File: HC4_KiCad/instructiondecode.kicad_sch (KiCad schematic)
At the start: 64 parts, among them IC18 74HC74, IC19 74HC32, IC20 74HC04, IC21 74HC00, IC22 74HC4053, IC23 74HC151, IC9 74HC4002

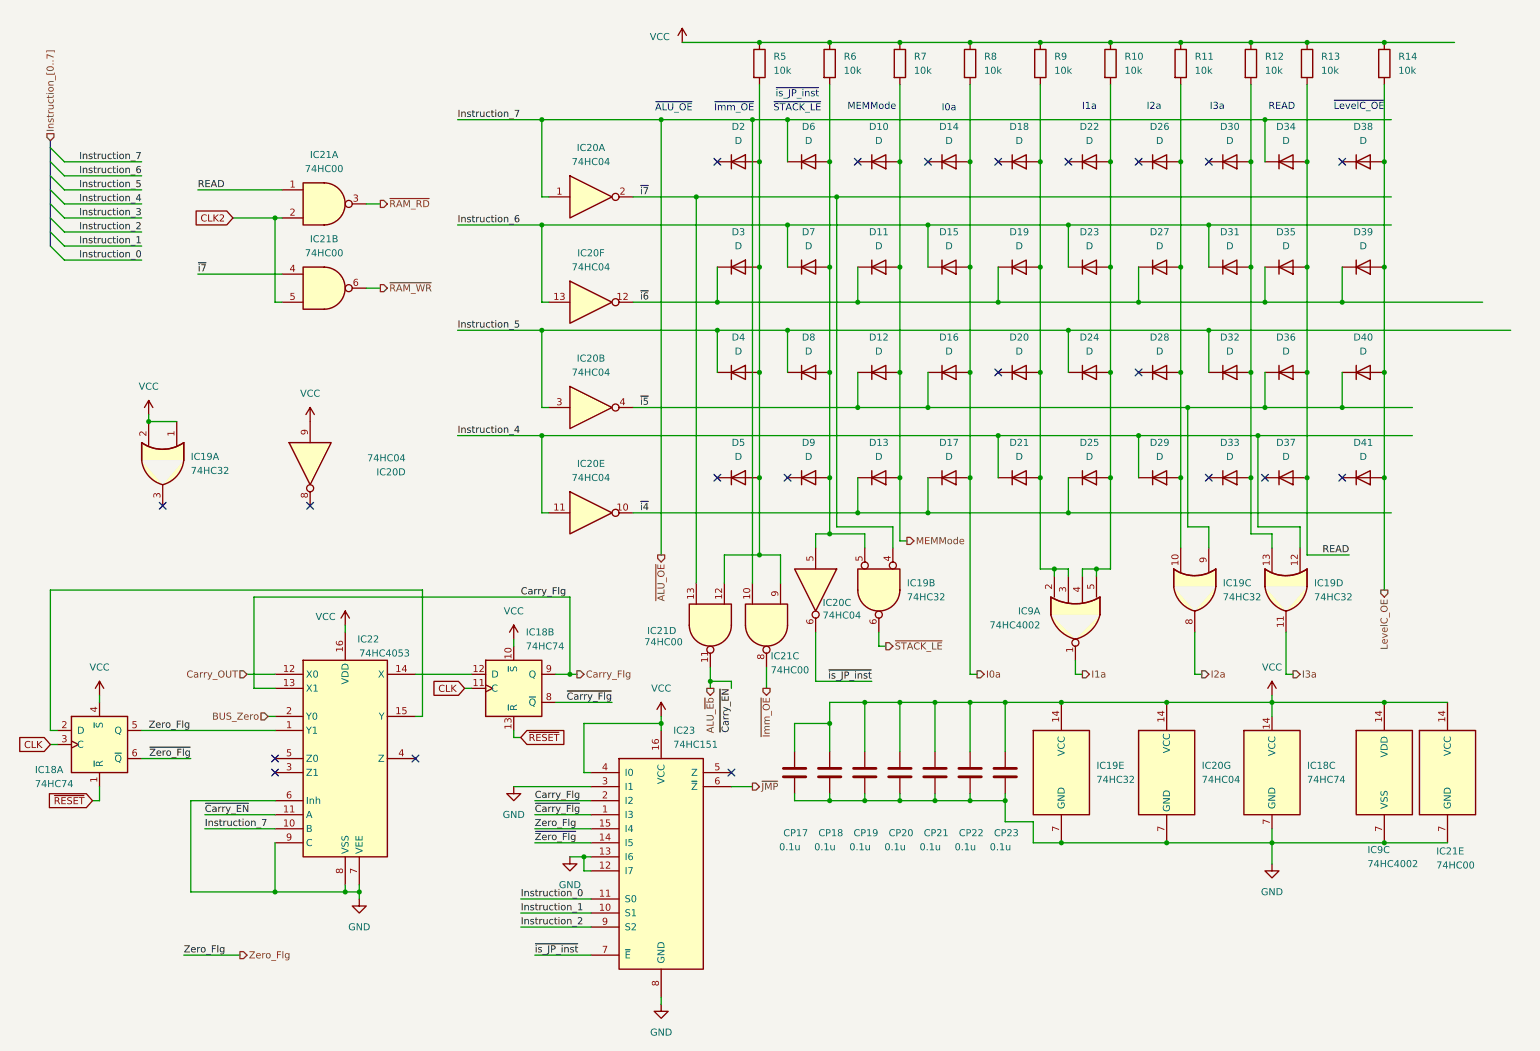
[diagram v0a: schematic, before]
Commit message: 部品配置完了
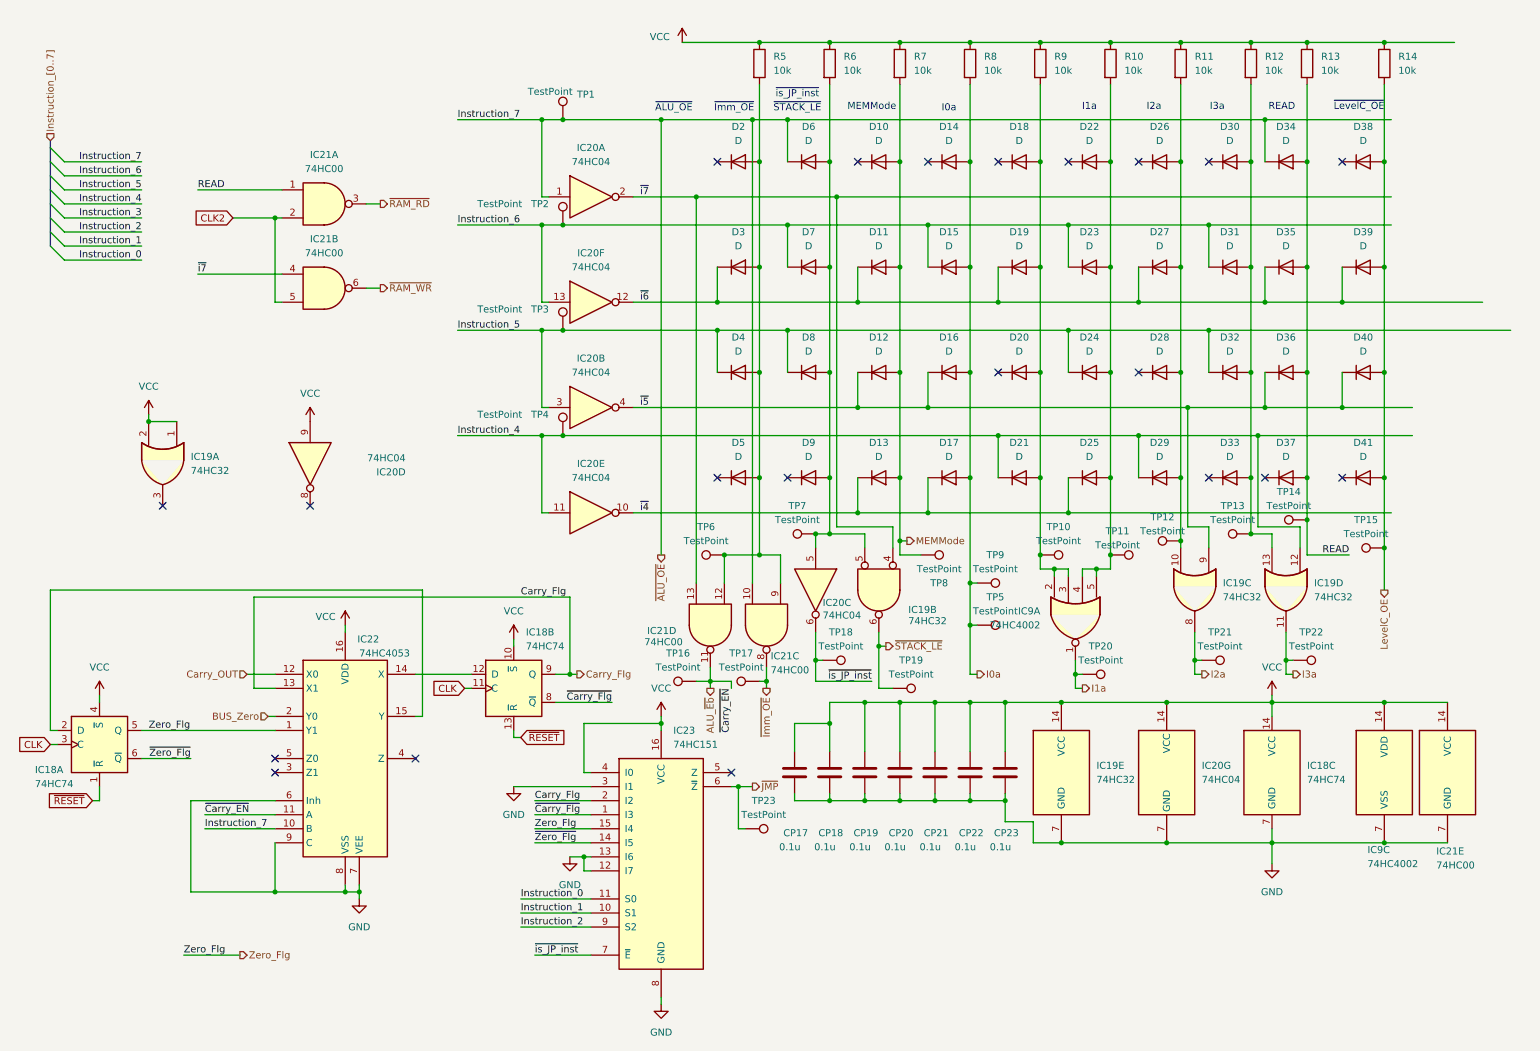
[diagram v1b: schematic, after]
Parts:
- added TP1, TP10, TP11, TP12, TP13, TP14, TP15, TP16, TP17, TP18, TP19, TP2, TP20, TP21, TP22, TP23, TP3, TP4, TP5, TP6, TP7, TP8, TP9: TestPoint, Library:TestPoint_THTPad_1.0x1.0mm_Drill0.5mm, symbol Connector:TestPoint
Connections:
- net ALU_~{Eb}: now also TP16.1
- net I0a: now also TP5.1, TP9.1
- net I1a: now also TP20.1
- net I2a: now also TP21.1
- net I3a: now also TP22.1
- net Instruction_4: now also TP4.1
- net Instruction_5: now also TP3.1
- net Instruction_6: now also TP2.1
- net LevelC_OE: now also TP15.1
- net MEMMode: now also TP8.1
- net READ: now also TP14.1
- net ~{ALU_OE}: now also TP1.1
- net ~{Imm_OE}: now also TP17.1
- net ~{JMP}: now also TP23.1
- net ~{STACK_LE}: now also TP19.1
- net ~{is_JP_inst}: now also TP18.1
- net at D26.2 (A), D27.2 (A), D28.2 (A)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: now also TP12.1
- net at D30.2 (A), D31.2 (A), D32.2 (A)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: now also TP13.1
- net at D2.2 (A), D3.2 (A), D4.2 (A)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: now also TP6.1
- net at D6.2 (A), D7.2 (A), D8.2 (A)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: now also TP7.1
- net at D22.2 (A), D23.2 (A), D24.2 (A)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: now also TP11.1
- net at D18.2 (A), D19.2 (A), D20.2 (A)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: now also TP10.1

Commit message: 配線完了とみられる
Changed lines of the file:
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@@
 (kicad_sch
-	(version 20231120)
+	(version 20250114)
 	(generator "eeschema")
-	(generator_version "8.0")
+	(generator_version "9.0")
 	(paper "A4")
 	(title_block
@@
 		(rev "1.3")
 	)
+	(text "I2a"
+		(exclude_from_sim no)
+		(at 219.964 28.194 0)
+		(effects
+			(font
+				(size 1.27 1.27)
+			)
+		)
+	)
+	(text "I0a"
+		(exclude_from_sim no)
+		(at 182.88 28.448 0)
+		(effects
+			(font
+				(size 1.27 1.27)
+			)
+		)
+	)
+	(text "~{Imm_OE}"
+		(exclude_from_sim no)
+		(at 144.018 28.448 0)
+		(effects
+			(font
+				(size 1.27 1.27)
+			)
+		)
+	)
+	(text "~{LevelC_OE}"
+		(exclude_from_sim no)
+		(at 257.048 28.194 0)
+		(effects
+			(font
+				(size 1.27 1.27)
+			)
+		)
+	)
+	(text "~{ALU_OE}"
+		(exclude_from_sim no)
+		(at 133.096 28.448 0)
+		(effects
+			(font
+				(size 1.27 1.27)
+			)
+		)
+	)
+	(text "~{STACK_LE}"
+		(exclude_from_sim no)
+		(at 155.448 28.448 0)
+		(effects
+			(font
+				(size 1.27 1.27)
+			)
+		)
+	)
+	(text "I3a"
+		(exclude_from_sim no)
+		(at 231.394 28.194 0)
+		(effects
+			(font
+				(size 1.27 1.27)
+			)
+		)
+	)
+	(text "READ"
+		(exclude_from_sim no)
+		(at 243.078 28.194 0)
+		(effects
+			(font
+				(size 1.27 1.27)
+			)
+		)
+	)
+	(text "MEMMode"
+		(exclude_from_sim no)
+		(at 168.91 28.194 0)
+		(effects
+			(font
+				(size 1.27 1.27)
+			)
+		)
+	)
+	(text "I1a"
+		(exclude_from_sim no)
+		(at 208.28 28.194 0)
+		(effects
+			(font
+				(size 1.27 1.27)
+			)
+		)
+	)
+	(text "~{is_JP_inst}"
+		(exclude_from_sim no)
+		(at 155.448 25.908 0)
+		(effects
+			(font
+				(size 1.27 1.27)
+			)
+		)
+	)
 	(junction
 		(at 167.64 135.89)
@@
 		)
 	)
-	(text "I2a"
-		(exclude_from_sim no)
-		(at 219.964 28.194 0)
-		(effects
-			(font
-				(size 1.27 1.27)
-			)
-		)
-	)
-	(text "I0a"
-		(exclude_from_sim no)
-		(at 182.88 28.448 0)
-		(effects
-			(font
-				(size 1.27 1.27)
-			)
-		)
-	)
-	(text "~{Imm_OE}"
-		(exclude_from_sim no)
-		(at 144.018 28.448 0)
-		(effects
-			(font
-				(size 1.27 1.27)
-			)
-		)
-	)
-	(text "~{LevelC_OE}"
-		(exclude_from_sim no)
-		(at 257.048 28.194 0)
-		(effects
-			(font
-				(size 1.27 1.27)
-			)
-		)
-	)
-	(text "~{ALU_OE}"
-		(exclude_from_sim no)
-		(at 133.096 28.448 0)
-		(effects
-			(font
-				(size 1.27 1.27)
-			)
-		)
-	)
-	(text "~{STACK_LE}"
-		(exclude_from_sim no)
-		(at 155.448 28.448 0)
-		(effects
-			(font
-				(size 1.27 1.27)
-			)
-		)
-	)
-	(text "I3a"
-		(exclude_from_sim no)
-		(at 231.394 28.194 0)
-		(effects
-			(font
-				(size 1.27 1.27)
-			)
-		)
-	)
-	(text "READ"
-		(exclude_from_sim no)
-		(at 243.078 28.194 0)
-		(effects
-			(font
-				(size 1.27 1.27)
-			)
-		)
-	)
-	(text "MEMMode"
-		(exclude_from_sim no)
-		(at 168.91 28.194 0)
-		(effects
-			(font
-				(size 1.27 1.27)
-			)
-		)
-	)
-	(text "I1a"
-		(exclude_from_sim no)
-		(at 208.28 28.194 0)
-		(effects
-			(font
-				(size 1.27 1.27)
-			)
-		)
-	)
-	(text "~{is_JP_inst}"
-		(exclude_from_sim no)
-		(at 155.448 25.908 0)
-		(effects
-			(font
-				(size 1.27 1.27)
-			)
-		)
-	)

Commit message: ミスを修正
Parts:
- removed unit 5 of IC21
- added unit 5 of IC5
- renumbered CP17 to CP1, CP18 to CP2, CP19 to CP3, CP20 to CP4, CP21 to CP5, CP22 to CP6, CP23 to CP7, D2 to D1, D11 to D10, D12 to D11, D13 to D12, D14 to D13, D15 to D14, D16 to D15, D17 to D16, D18 to D17, D19 to D18, D20 to D19, D3 to D2, D21 to D20, D22 to D21, D23 to D22, D24 to D23, D25 to D24, D26 to D25, D27 to D26, D28 to D27, D29 to D28, D30 to D29, D4 to D3, D31 to D30, D32 to D31, D33 to D32, D34 to D33, D35 to D34, D36 to D35, D37 to D36, D38 to D37, D39 to D38, D40 to D39, D5 to D4, D41 to D40, D6 to D5, D7 to D6, D8 to D7, D9 to D8, D10 to D9, IC18 to IC2, IC19 to IC3, IC20 to IC4, IC21 to IC5, IC22 to IC6, IC23 to IC7, IC9 to IC8, R5 to R1, R14 to R10, R6 to R2, R7 to R3, R8 to R4, R9 to R5, R10 to R6, R11 to R7, R12 to R8, R13 to R9, TP18 to TP10, TP19 to TP11, TP8 to TP12, TP9 to TP13, TP5 to TP14, TP10 to TP15, TP20 to TP16, TP11 to TP17, TP12 to TP18, TP21 to TP19, TP13 to TP20, TP22 to TP21, TP14 to TP22, TP15 to TP23, TP16 to TP5, TP23 to TP7, TP17 to TP8, TP7 to TP9
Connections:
- net ALU_~{Eb}: now also IC5.3; no longer IC5.11
- net CLK2: now also IC5.10, IC5.13; no longer IC5.2, IC5.5
- net GND: now also IC5.7 (GND)
- net Instruction_5: now also D15.1 (K)
- net Instruction_6: no longer D14.1 (K)
- net READ: now also IC5.9; no longer IC5.1
- net VCC: now also IC4.5, IC5.14 (VCC); no longer IC4.9
- net ~{ALU_OE}: now also IC5.5; no longer IC5.10
- net ~{Imm_OE}: now also IC5.6; no longer IC5.8
- net ~{RAM_RD}: now also IC5.8; no longer IC5.3
- net ~{RAM_WR}: now also IC5.11; no longer IC5.6
- net ~{i5}: no longer D15.1 (K)
- net ~{i6}: now also D14.1 (K)
- net ~{i7}: now also IC5.12, IC5.2; no longer IC5.13, IC5.4
- net ~{is_JP_inst}: now also IC4.8; no longer IC4.6
- net at D1.2 (A), D2.2 (A), D3.2 (A)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: now also IC5.1, IC5.4; no longer IC5.12, IC5.9
- net at D5.2 (A), D6.2 (A), D7.2 (A)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: now also IC4.9; no longer IC4.5

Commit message: なんか変わってた
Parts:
- renumbered CP1 to CP17, CP2 to CP18, CP3 to CP19, CP4 to CP20, CP5 to CP21, CP6 to CP22, CP7 to CP23, D9 to D10, D10 to D11, D11 to D12, D12 to D13, D13 to D14, D14 to D15, D15 to D16, D16 to D17, D17 to D18, D18 to D19, D1 to D2, D19 to D20, D20 to D21, D21 to D22, D22 to D23, D23 to D24, D24 to D25, D25 to D26, D26 to D27, D27 to D28, D28 to D29, D2 to D3, D29 to D30, D30 to D31, D31 to D32, D32 to D33, D33 to D34, D34 to D35, D35 to D36, D36 to D37, D37 to D38, D38 to D39, D3 to D4, D39 to D40, D40 to D41, D4 to D5, D5 to D6, D6 to D7, D7 to D8, D8 to D9, IC2 to IC18, IC3 to IC19, IC4 to IC20, IC5 to IC21, IC6 to IC22, IC7 to IC23, IC8 to IC9, R6 to R10, R7 to R11, R8 to R12, R9 to R13, R10 to R14, R1 to R5, R2 to R6, R3 to R7, R4 to R8, R5 to R9
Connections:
- net ALU_~{Eb}: now also IC21.11; no longer IC21.3
- net CLK2: now also IC21.2, IC21.5; no longer IC21.10, IC21.13
- net READ: now also IC21.1; no longer IC21.9
- net VCC: now also IC20.9; no longer IC20.5
- net ~{ALU_OE}: now also IC21.10; no longer IC21.5
- net ~{Imm_OE}: now also IC21.8; no longer IC21.6
- net ~{RAM_RD}: now also IC21.3; no longer IC21.8
- net ~{RAM_WR}: now also IC21.6; no longer IC21.11
- net ~{i7}: now also IC21.13, IC21.4; no longer IC21.12, IC21.2
- net ~{is_JP_inst}: now also IC20.6; no longer IC20.8
- net at D2.2 (A), D3.2 (A), D4.2 (A)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: now also IC21.12, IC21.9; no longer IC21.1, IC21.4
- net at D6.2 (A), D7.2 (A), D8.2 (A)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: now also IC20.5; no longer IC20.9

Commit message: moti
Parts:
- removed R10, R11, R12, R5, R6, R7, R8, R9: 10k, Resistor_SMD:R_0603_1608Metric, symbol Device:R
- added RN7: 10k, Resistor_THT:R_Array_SIP9, symbol Device:R_Network08_Split
- IC17: renamed from IC18; footprint Package_SO:SO-14_5.3x10.2mm_P1.27mm -> Package_DIP:DIP-14_W7.62mm
- IC18: renamed from IC19; footprint Package_SO:SO-14_5.3x10.2mm_P1.27mm -> Package_DIP:DIP-14_W7.62mm
- IC19: renamed from IC20; footprint Package_SO:SO-14_5.3x10.2mm_P1.27mm -> Package_DIP:DIP-14_W7.62mm
- IC20: renamed from IC21; footprint Package_SO:SO-14_5.3x10.2mm_P1.27mm -> Package_DIP:DIP-14_W7.62mm
- IC21: renamed from IC22; footprint Package_SO:SO-16_5.3x10.2mm_P1.27mm -> Package_DIP:DIP-16_W7.62mm
- IC22: renamed from IC23; footprint Package_SO:SO-16_5.3x10.2mm_P1.27mm -> Package_DIP:DIP-16_W7.62mm
- IC8: renamed from IC9; footprint Package_SO:SO-14_5.3x10.2mm_P1.27mm -> Package_DIP:DIP-14_W7.62mm
- renumbered CP17 to CP16, CP18 to CP17, CP19 to CP18, CP20 to CP19, CP21 to CP20, CP22 to CP21, CP23 to CP22, R13 to R5, R14 to R6
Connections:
- net I0a: now also RN7.5 (R4.2)
- net MEMMode: now also RN7.4 (R3.2)
- net VCC: now also RN7.1 (R1), RN7.1 (R1), RN7.1 (R1), RN7.1 (R1), RN7.1 (R1), RN7.1 (R1), RN7.1 (R1), RN7.1 (R1)
- net at D26.2 (A), D27.2 (A), D28.2 (A)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: now also RN7.8 (R7.2)
- net at D30.2 (A), D31.2 (A), D32.2 (A)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: now also RN7.9 (R8.2)
- net at D2.2 (A), D3.2 (A), D4.2 (A)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: now also RN7.2 (R1.2)
- net at D6.2 (A), D7.2 (A), D8.2 (A)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: now also RN7.3 (R2.2)
- net at D22.2 (A), D23.2 (A), D24.2 (A)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: now also RN7.7 (R6.2)
- net at D18.2 (A), D19.2 (A), D20.2 (A)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: now also RN7.6 (R5.2)

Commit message: 基板途中
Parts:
- removed TP12, TP13, TP15, TP17, TP18, TP20, TP22, TP23, TP6, TP9: TestPoint, Library:TestPoint_THTPad_1.0x1.0mm_Drill0.5mm, symbol Connector:TestPoint
- renumbered CP16 to CP15, CP17 to CP16, CP18 to CP17, CP19 to CP18, CP20 to CP19, CP21 to CP20, CP22 to CP21, D2 to D1, D11 to D10, D12 to D11, D13 to D12, D14 to D13, D15 to D14, D16 to D15, D17 to D16, D18 to D17, D19 to D18, D20 to D19, D3 to D2, D21 to D20, D22 to D21, D23 to D22, D24 to D23, D25 to D24, D26 to D25, D27 to D26, D28 to D27, D29 to D28, D30 to D29, D4 to D3, D31 to D30, D32 to D31, D33 to D32, D34 to D33, D35 to D34, D36 to D35, D37 to D36, D38 to D37, D39 to D38, D40 to D39, D5 to D4, D41 to D40, D6 to D5, D7 to D6, D8 to D7, D9 to D8, D10 to D9, TP14 to TP10, TP16 to TP11, TP19 to TP12, TP21 to TP13, TP7 to TP6, TP8 to TP7, TP10 to TP8, TP11 to TP9

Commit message: 仮
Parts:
- renumbered IC17 to IC16, IC18 to IC17, IC19 to IC18, IC20 to IC19, IC21 to IC20, IC22 to IC21
